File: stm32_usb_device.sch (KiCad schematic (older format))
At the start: 0 parts

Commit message: Add USB connector, protection diodes and MCU
Signed-off-by: Tomislav Milkovic <tomislav.milkovic95@gmail.com>
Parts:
- added C? (x2): 10u, symbol Device:C_Small
- added J?: USB_A, symbol Connector:USB_A
- added U?: STM32F103C8T6, Package_QFP:LQFP-48_7x7mm_P0.5mm, symbol MCU_ST_STM32F1:STM32F103C8Tx
- added U?: HT7533-1, Package_TO_SOT_SMD:SOT-89-3, symbol Regulator_Linear:HT75xx-1-SOT89
- added U?: SRV05-4, Package_TO_SOT_SMD:SOT-23-6, symbol Power_Protection:SRV05-4
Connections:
- new net +3V3: C?.1, U?.3 (VOUT)
- new net +5V: C?.1, J?.1 (VBUS), U?.2 (VIN), U?.5 (VP)
- new net GND: C?.2, C?.2, J?.4 (GND), U?.1 (GND), U?.2 (VN)
- new net USB_D+: J?.3 (D+), U?.1 (IO1), U?.6 (IO4)
- new net USB_D-: J?.2 (D-), U?.3 (IO2), U?.4 (IO3)
- no-connect marks 0 -> 1
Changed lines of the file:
@@
 Comment4 ""
 $EndDescr
+$Comp
+L MCU_ST_STM32F1:STM32F103C8Tx U?
+U 1 1 6593FE3E
+P 4475 5100
+F 0 "U?" H 4925 6575 50  0000 C CNN
+F 1 "STM32F103C8T6" H 4950 3625 50  0000 C CNN
+F 2 "Package_QFP:LQFP-48_7x7mm_P0.5mm" H 3875 3700 50  0001 R CNN
+F 3 "http://www.st.com/st-web-ui/static/active/en/resource/technical/document/datasheet/CD00161566.pdf" H 4475 5100 50  0001 C CNN
+	1    4475 5100
+	1    0    0    -1
+$EndComp
+$Comp
+L Regulator_Linear:HT75xx-1-SOT89 U?
+U 1 1 6594370E
+P 4100 1025
+F 0 "U?" H 4225 1275 39  0000 C CNN
+F 1 "HT7533-1" H 4300 875 39  0000 C CNN
+F 2 "Package_TO_SOT_SMD:SOT-89-3" H 4100 1350 50  0001 C CIN
+F 3 "https://www.holtek.com/documents/10179/116711/HT75xx-1v250.pdf" H 4100 1125 50  0001 C CNN
+	1    4100 1025
+	1    0    0    -1
+$EndComp
+$Comp
+L Power_Protection:SRV05-4 U?
+U 1 1 65944C18
+P 4100 2600
+F 0 "U?" H 4350 3050 39  0000 C CNN
+F 1 "SRV05-4" H 4350 2150 39  0000 C CNN
+F 2 "Package_TO_SOT_SMD:SOT-23-6" H 4800 2150 50  0001 C CNN
+F 3 "http://www.onsemi.com/pub/Collateral/SRV05-4-D.PDF" H 4100 2600 50  0001 C CNN
+	1    4100 2600
+	1    0    0    -1
+$EndComp
+Text Label 2200 2050 2    39   ~ 0
+USB_D+
+Text Label 2200 2150 2    39   ~ 0
+USB_D-
+Wire Wire Line
+	1975 2050 2200 2050
+Wire Wire Line
+	1975 2150 2200 2150
+$Comp
+L power:GND #PWR?
+U 1 1 659470E1
+P 1675 2450
+F 0 "#PWR?" H 1675 2200 50  0001 C CNN
+F 1 "GND" H 1675 2300 39  0000 C CNN
+F 2 "" H 1675 2450 50  0001 C CNN
+F 3 "" H 1675 2450 50  0001 C CNN
+	1    1675 2450
+	1    0    0    -1
+$EndComp
+Text Label 3375 2500 0    39   ~ 0
+USB_D+
+Text Label 4825 2700 2    39   ~ 0
+USB_D+
+Text Label 4825 2500 2    39   ~ 0
+USB_D-
+Text Label 3375 2700 0    39   ~ 0
+USB_D-
+$Comp
+L power:GND #PWR?
+U 1 1 65948045
+P 4100 3100
+F 0 "#PWR?" H 4100 2850 50  0001 C CNN
+F 1 "GND" H 4100 2950 39  0000 C CNN
+F 2 "" H 4100 3100 50  0001 C CNN
+F 3 "" H 4100 3100 50  0001 C CNN
+	1    4100 3100
+	1    0    0    -1
+$EndComp
+$Comp
+L power:+5V #PWR?
+U 1 1 65948BF7
+P 4100 2100
+F 0 "#PWR?" H 4100 1950 50  0001 C CNN
+F 1 "+5V" H 4100 2250 39  0000 C CNN
+F 2 "" H 4100 2100 50  0001 C CNN
+F 3 "" H 4100 2100 50  0001 C CNN
+	1    4100 2100
+	1    0    0    -1
+$EndComp
+$Comp
+L power:GND #PWR?
+U 1 1 6594DD6F
+P 4100 1350
+F 0 "#PWR?" H 4100 1100 50  0001 C CNN
+F 1 "GND" H 4105 1185 39  0000 C CNN
+F 2 "" H 4100 1350 50  0001 C CNN
+F 3 "" H 4100 1350 50  0001 C CNN
+	1    4100 1350
+	1    0    0    -1
+$EndComp
+$Comp
+L Connector:USB_A J?
+U 1 1 65943F4E
+P 1675 2050
+F 0 "J?" H 1850 2400 39  0000 C CNN
+F 1 "USB_A" H 1825 1700 39  0000 C CNN
+F 2 "" H 1825 2000 50  0001 C CNN
+F 3 " ~" H 1825 2000 50  0001 C CNN
+	1    1675 2050
+	1    0    0    -1
+$EndComp
+NoConn ~ 1575 2450
+Wire Wire Line
+	1975 1850 2200 1850
+Wire Wire Line
+	2200 1850 2200 1800
+$Comp
+L power:+5V #PWR?
+U 1 1 65950B2F
+P 2200 1800
+F 0 "#PWR?" H 2200 1650 50  0001 C CNN
+F 1 "+5V" H 2200 1950 39  0000 C CNN
+F 2 "" H 2200 1800 50  0001 C CNN
+F 3 "" H 2200 1800 50  0001 C CNN
+	1    2200 1800
+	1    0    0    -1
+$EndComp
+$Comp
+L power:+3.3V #PWR?
+U 1 1 65951F1A
+P 4725 850
+F 0 "#PWR?" H 4725 700 50  0001 C CNN
+F 1 "+3.3V" H 4740 1015 39  0000 C CNN
+F 2 "" H 4725 850 50  0001 C CNN
+F 3 "" H 4725 850 50  0001 C CNN
+	1    4725 850
+	1    0    0    -1
+$EndComp
+Wire Wire Line
+	4725 925  4725 850
+Wire Wire Line
+	4400 925  4650 925
+Wire Wire Line
+	3800 925  3550 925
+Wire Wire Line
+	3475 925  3475 850
+$Comp
+L power:+5V #PWR?
+U 1 1 65953409
+P 3475 850
+F 0 "#PWR?" H 3475 700 50  0001 C CNN
+F 1 "+5V" H 3490 1015 39  0000 C CNN
+F 2 "" H 3475 850 50  0001 C CNN
+F 3 "" H 3475 850 50  0001 C CNN
+	1    3475 850
+	1    0    0    -1
+$EndComp
+$Comp
+L Device:C_Small C?
+U 1 1 65953C6A
+P 3550 1025
+F 0 "C?" H 3625 1050 39  0000 L CNN
+F 1 "10u" H 3600 975 39  0000 L CNN
+F 2 "" H 3550 1025 50  0001 C CNN
+F 3 "~" H 3550 1025 50  0001 C CNN
+	1    3550 1025
+	1    0    0    -1
+$EndComp
+Connection ~ 3550 925
+Wire Wire Line
+	3550 925  3475 925
+$Comp
+L Device:C_Small C?
+U 1 1 659551DC
+P 4650 1025
+F 0 "C?" H 4725 1025 39  0000 L CNN
+F 1 "10u" H 4725 975 39  0000 L CNN
+F 2 "" H 4650 1025 50  0001 C CNN
+F 3 "~" H 4650 1025 50  0001 C CNN
+	1    4650 1025
+	1    0    0    -1
+$EndComp
+Connection ~ 4650 925
+Wire Wire Line
+	4650 925  4725 925
+Wire Wire Line
+	4100 1225 4100 1300
+Wire Wire Line
+	4650 1125 4650 1300
+Wire Wire Line
+	4650 1300 4100 1300
+Connection ~ 4100 1300
+Wire Wire Line
+	4100 1300 4100 1350
+Wire Wire Line
+	4100 1300 3550 1300
+Wire Wire Line
+	3550 1300 3550 1125
+Wire Wire Line
+	4600 2500 4825 2500
+Wire Wire Line
+	4600 2700 4825 2700
+Wire Wire Line
+	3600 2500 3375 2500
+Wire Wire Line
+	3600 2700 3375 2700
+Wire Notes Line
+	7525 3375 7525 500
+Wire Notes Line
+	7525 500  500  500
+Wire Notes Line
+	7525 3375 500  3375
+Wire Notes Line
+	500  500  500  3375
+Wire Notes Line
+	2775 500  2775 3375
+Wire Notes Line
+	2775 1725 7525 1725
 $EndSCHEMATC

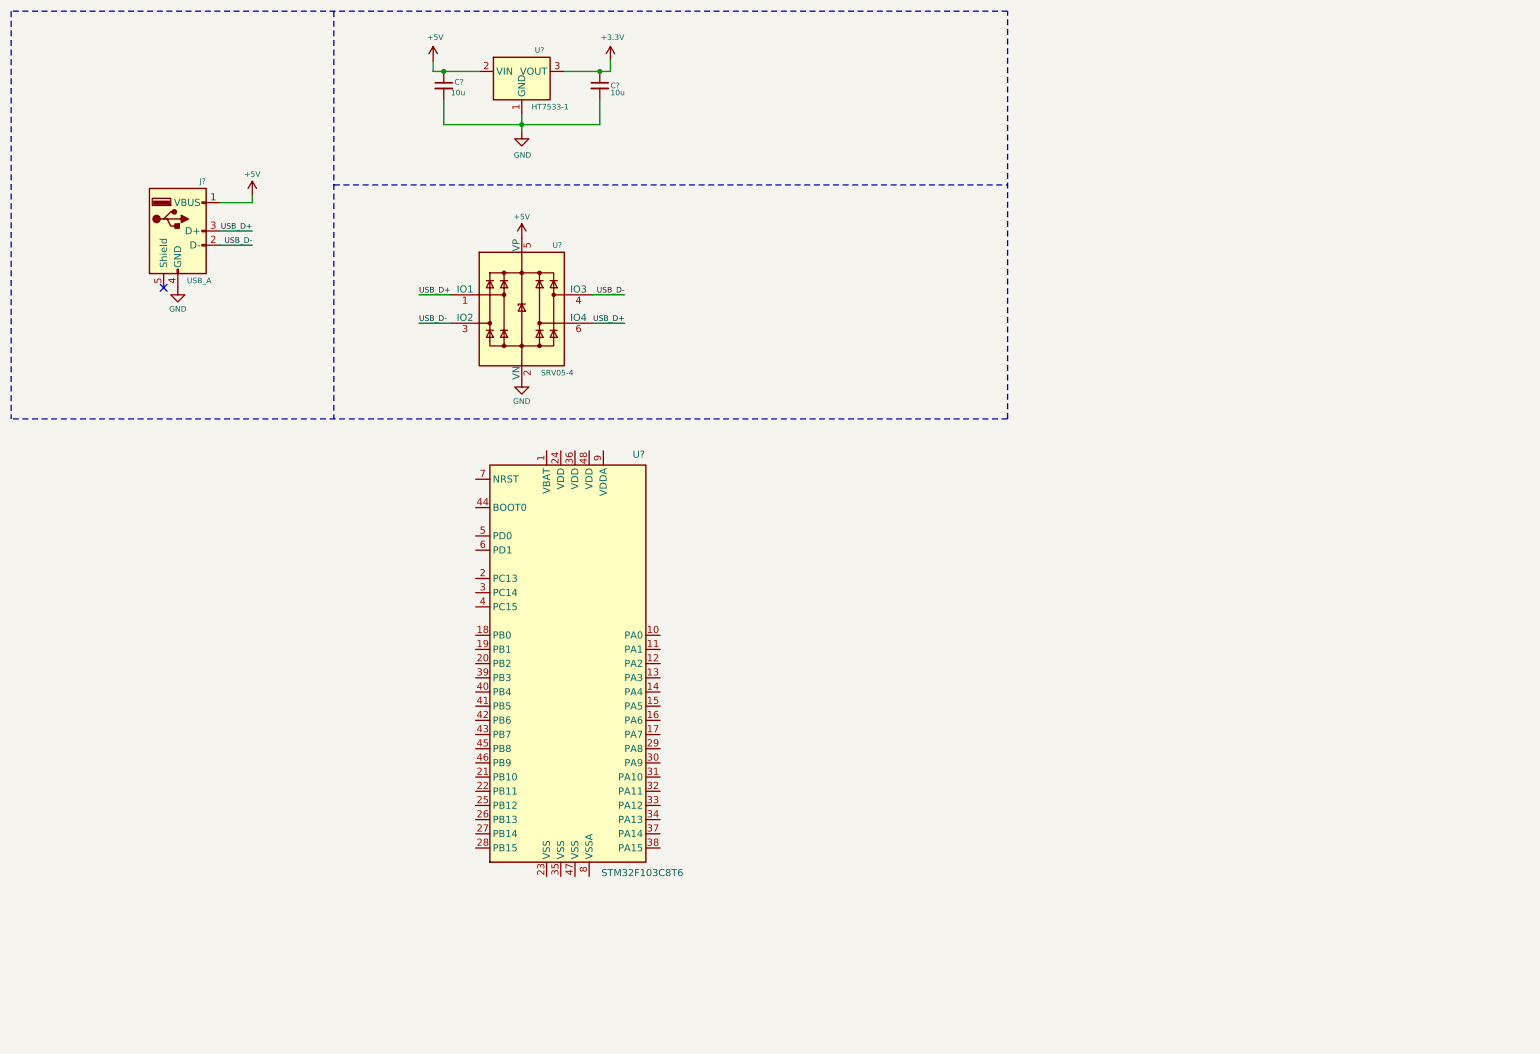
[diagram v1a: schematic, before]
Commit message: schematic: Add power supply, decoupling caps, pin headers
Signed-off-by: Tomislav Milkovic <tomislav.milkovic95@gmail.com>
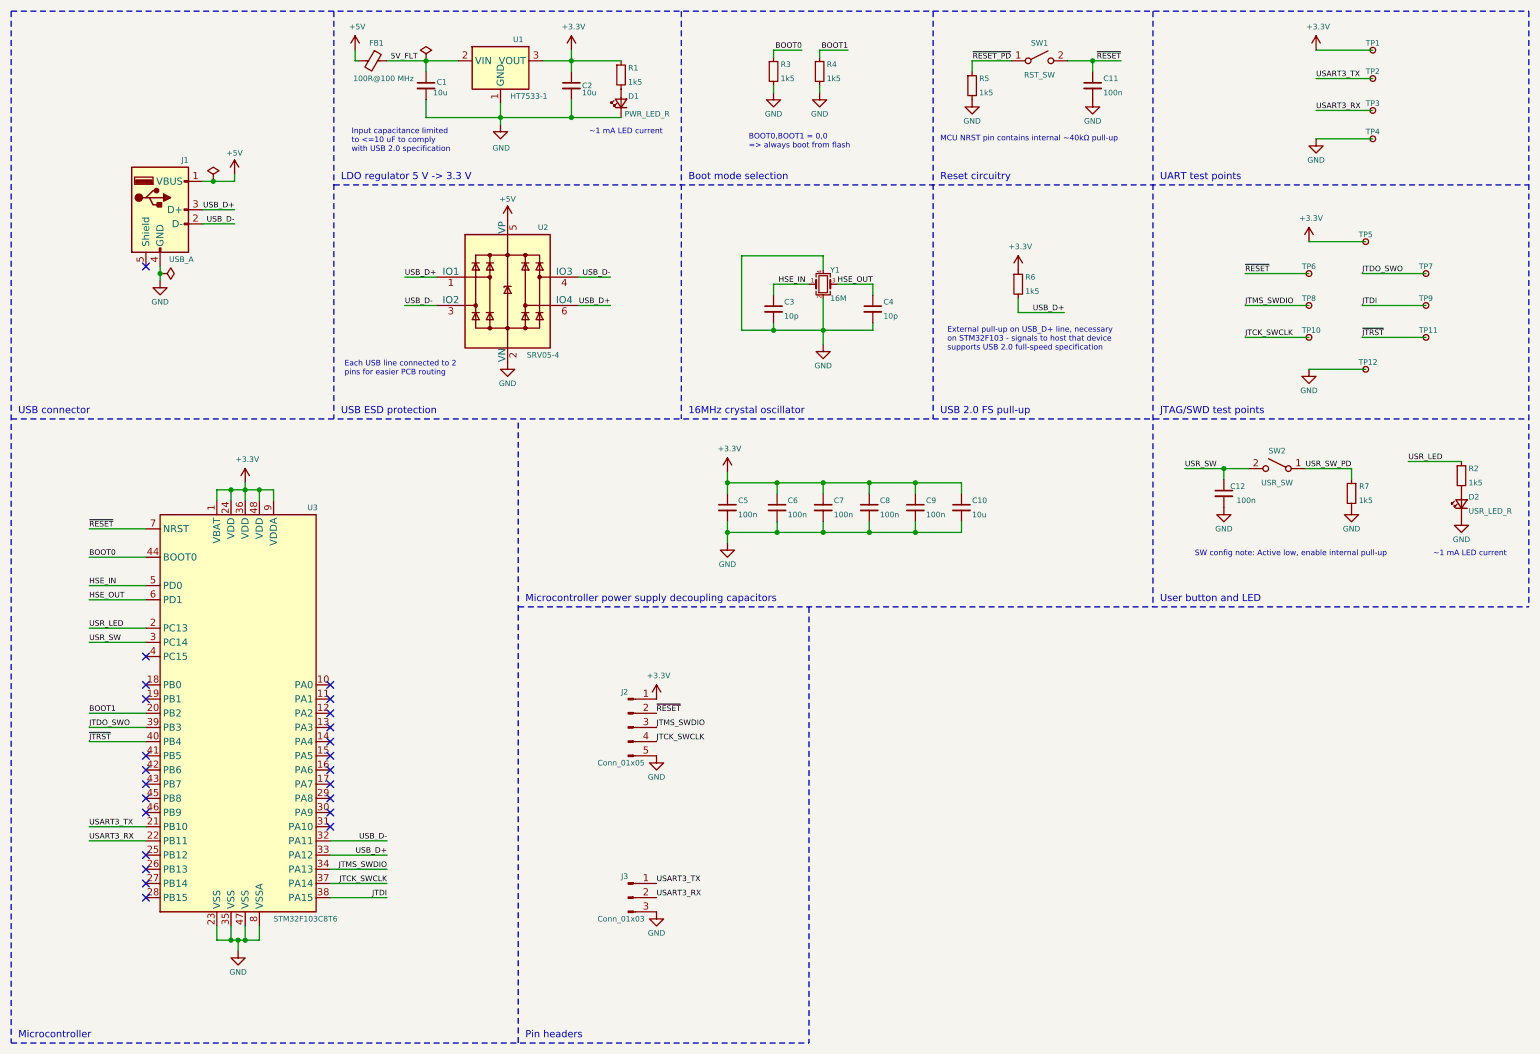
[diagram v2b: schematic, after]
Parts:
- added C10: 10u, Capacitor_SMD:C_0603_1608Metric, symbol Device:C_Small
- added C11, C12, C5, C6, C7, C8, C9: 100n, Capacitor_SMD:C_0402_1005Metric, symbol Device:C_Small
- added C3, C4: 10p, Capacitor_SMD:C_0402_1005Metric, symbol Device:C_Small
- added D1: PWR_LED_R, LED_SMD:LED_0603_1608Metric, symbol Device:LED_Small
- added D2: USR_LED_R, LED_SMD:LED_0603_1608Metric, symbol Device:LED_Small
- added FB1: 100R@100 MHz, Inductor_SMD:L_0805_2012Metric, symbol Device:Ferrite_Bead_Small
- added J2: Conn_01x05, Connector_PinHeader_2.54mm:PinHeader_1x05_P2.54mm_Vertical, symbol Connector:Conn_01x05_Male
- added J3: Conn_01x03, Connector_PinHeader_2.54mm:PinHeader_1x03_P2.54mm_Vertical, symbol Connector:Conn_01x03_Male
- added R1, R2, R3, R4, R5, R6, R7: 1k5, Resistor_SMD:R_0402_1005Metric, symbol Device:R_Small
- added SW1: RST_SW, Button_Switch_SMD:SW_SPST_CK_RS282G05A3, symbol Switch:SW_SPST
- added SW2: USR_SW, Button_Switch_SMD:SW_SPST_CK_RS282G05A3, symbol Switch:SW_SPST
- added TP1, TP10, TP11, TP12, TP2, TP3, TP4, TP5, TP6, TP7, TP8, TP9: TestPoint_Small, TestPoint:TestPoint_Pad_D1.0mm, symbol Connector:TestPoint_Small
- added Y1: 16M, Crystal:Crystal_SMD_3225-4Pin_3.2x2.5mm, symbol Device:Crystal_GND24_Small
- C1, C2: renamed from C?; footprint (none) -> Capacitor_SMD:C_0603_1608Metric
- J1: renamed from J?; footprint (none) -> Connector_USB:USB_A_CNCTech_1001-011-01101_Horizontal
- gave numbers to parts that had none: 3
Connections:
- net +3V3: now also U3.1 (VBAT), U3.24 (VDD), U3.36 (VDD), U3.48 (VDD), U3.9 (VDDA), C10.1, C5.1, C6.1, C7.1, C8.1, C9.1, J2.1 (Pin_1), R1.1, R6.1, TP1.1, TP5.1
- net +5V: now also FB1.2; no longer C1.1, U1.2 (VIN)
- net GND: now also U3.23 (VSS), U3.35 (VSS), U3.47 (VSS), U3.8 (VSSA), C10.2, C11.2, C12.2, C3.2, C4.2, C5.2, C6.2, C7.2, C8.2, C9.2, D1.1 (K), D2.1 (K), J2.5 (Pin_5), J3.3 (Pin_3), R3.2, R4.2, R5.2, R7.2, TP12.1, TP4.1, Y1.2, Y1.4
- net USB_D+: now also U3.33 (PA12), R6.2
- net USB_D-: now also U3.32 (PA11)
- net USR_LED: now reaches U3.2 (PC13)
- net USR_LED: now also R2.1
- net BOOT1: now reaches U3.20 (PB2)
- net BOOT1: now also R4.1
- net USART3_TX: now reaches U3.21 (PB10)
- net USART3_TX: now also J3.1 (Pin_1), TP2.1
- net USART3_RX: now reaches U3.22 (PB11)
- net USART3_RX: now also J3.2 (Pin_2), TP3.1
- net USR_SW: now reaches U3.3 (PC14)
- net USR_SW: now also C12.1, SW2.2 (B)
- net JTMS_SWDIO: now reaches U3.34 (PA13)
- net JTMS_SWDIO: now also J2.3 (Pin_3), TP8.1
- net JTCK_SWCLK: now reaches U3.37 (PA14)
- net JTCK_SWCLK: now also J2.4 (Pin_4), TP10.1
- net JTDI: now reaches U3.38 (PA15)
- net JTDI: now also TP9.1
- net JTDO_SWO: now reaches U3.39 (PB3)
- net JTDO_SWO: now also TP7.1
- net ~JTRST: now reaches U3.40 (PB4)
- net ~JTRST: now also TP11.1
- net BOOT0: now reaches U3.44 (BOOT0)
- net BOOT0: now also R3.1
- net HSE_IN: now reaches U3.5 (PD0)
- net HSE_IN: now also C3.1, Y1.1
- net HSE_OUT: now reaches U3.6 (PD1)
- net HSE_OUT: now also C4.1, Y1.3
- net ~RESET: now reaches U3.7 (NRST)
- net ~RESET: now also C11.1, J2.2 (Pin_2), SW1.2 (B), TP6.1
- new net: D1.2 (A), R1.2
- new net: D2.2 (A), R2.2
- new net 5V_FLT: C1.1, FB1.1, U1.2 (VIN)
- new net USR_SW_PD: R7.1, SW2.1 (A)
- new net ~RESET_PD: R5.1, SW1.1 (A)
- no-connect marks 1 -> 24
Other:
- note added: "16MHz crystal oscillator"
- note added: "BOOT0,BOOT1 = 0,0\n=> always boot from flash"
- note added: "Boot mode selection"
- note added: "Each USB line connected to 2\npins for easier PCB routing"
- note added: "External pull-up on USB_D+ line, necessary\non STM32F103 - signals to host that device\nsupports USB 2.0 full-speed specification"
- note added: "Input capacitance limited\nto <=10 uF to comply\nwith USB 2.0 specification"
- note added: "JTAG/SWD test points"
- note added: "LDO regulator 5 V -> 3.3 V"
- note added: "MCU NRST pin contains internal ~~40kΩ pull-up"
- note added: "Microcontroller"
- note added: "Microcontroller power supply decoupling capacitors"
- note added: "Pin headers"
- note added: "Reset circuitry"
- note added: "SW config note: Active low, enable internal pull-up"
- note added: "UART test points"
- note added: "USB 2.0 FS pull-up"
- note added: "USB ESD protection"
- note added: "USB connector"
- note added: "User button and LED"
- note added: "~~1 mA LED current"
- moved on the sheet: C1, C2, J1, U1, U2, U3
